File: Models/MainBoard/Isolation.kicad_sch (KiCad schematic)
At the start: 0 parts

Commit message: Save progress
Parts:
- added U2: ISO7761DW, symbol Vendor:ISO7761DW
- added U3: ISO1641DW, symbol Vendor:ISO1641DW
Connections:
- new net 3.3V_Analog: U2.16 (VCC2)
- new net 3.3V_Digital: U2.1 (VCC1), U3.3 (VCC1)
- new net 5V_Analog: U3.14 (VCC2)
- new net CS1_Analog: U2.13 (OUTC)
- new net CS1_Digital: U2.4 (INC)
- new net CS2_Analog: U2.14 (OUTB)
- new net CS2_Digital: U2.3 (INB)
- new net CS3_Analog: U2.15 (OUTA)
- new net CS3_Digital: U2.2 (INA)
- new net GND_Analog: U2.9 (GND2), U3.16 (GND2), U3.9 (GND2)
- new net GND_Digital: U2.8 (GND1), U3.1 (GND1), U3.7 (GND1)
- new net MISO_Analog: U2.10 (INF)
- new net MISO_Digital: U2.7 (OUTF)
- new net MOSI_Analog: U2.12 (OUTD)
- new net MOSI_Digital: U2.5 (IND)
- new net SCK_Analog: U2.11 (OUTE)
- new net SCK_Digital: U2.6 (INE)
- new net SCL_Analog: U3.11 (SCL2)
- new net SCL_Digital: U3.6 (SCL2)
- new net SDA_Analog: U3.12 (SDA2)
- new net SDA_Digital: U3.5 (SDA1)
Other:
- note added: "Analog / High Voltage"
- note added: "Digital"

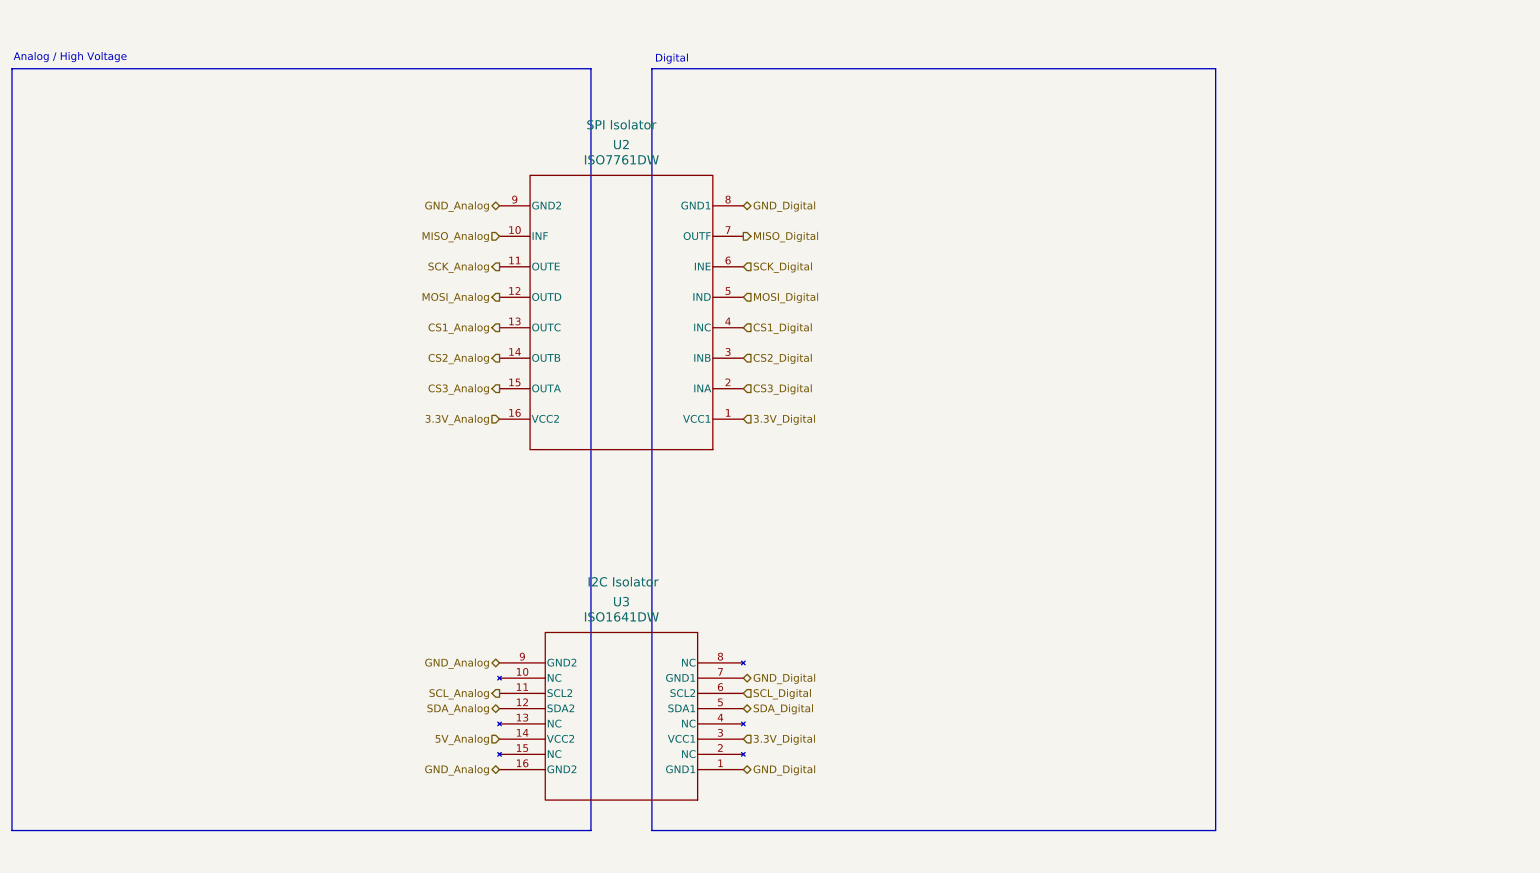
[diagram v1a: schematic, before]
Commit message: Finished the isolators
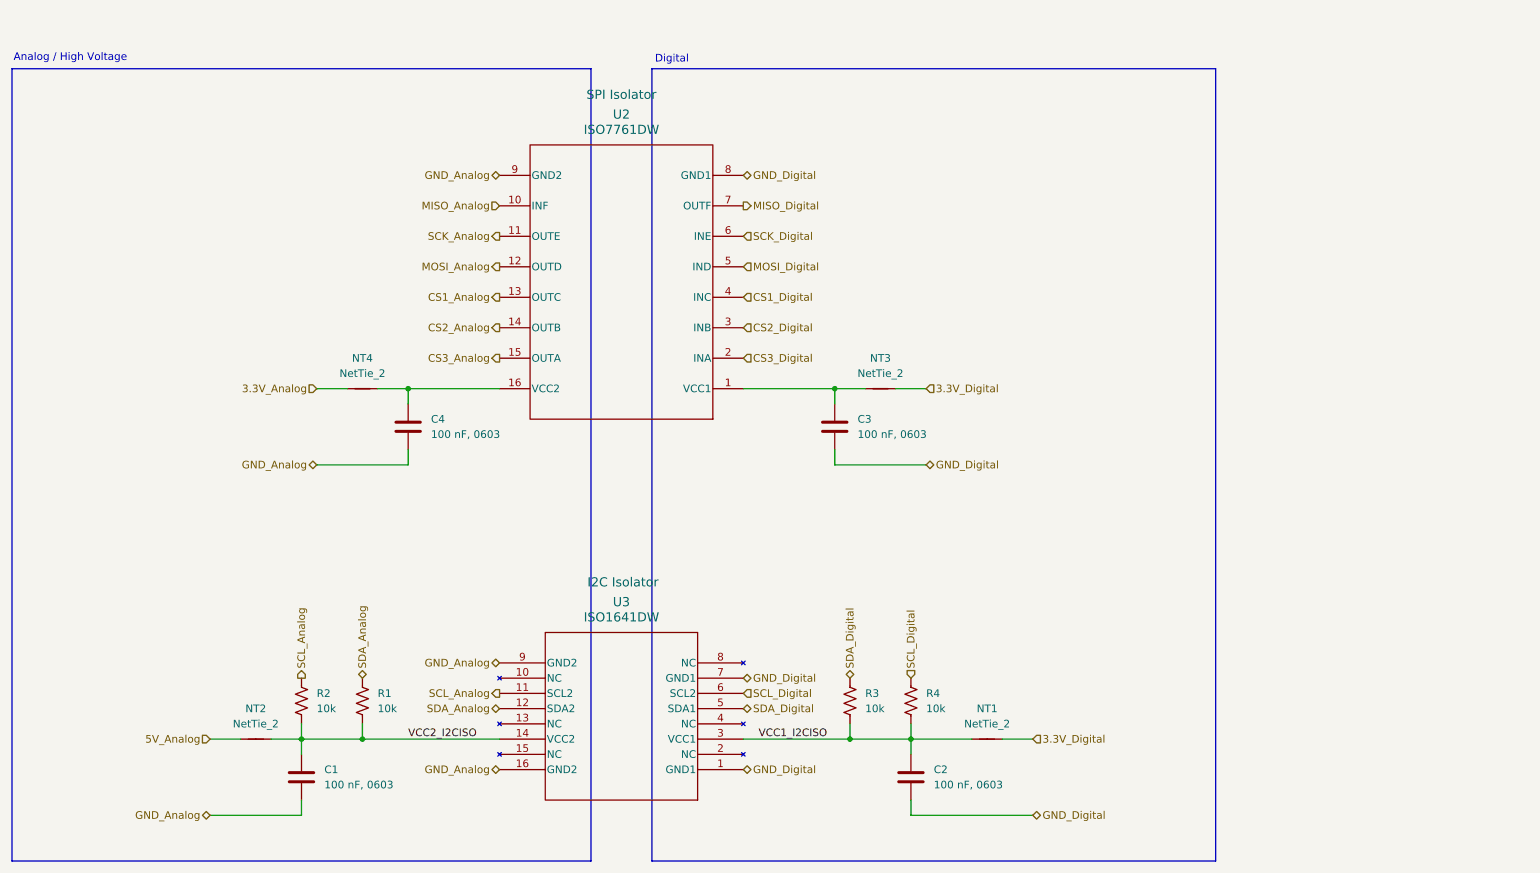
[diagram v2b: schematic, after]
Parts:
- added C1, C2, C3, C4: 100 nF, 0603, symbol Device:C
- added NT1, NT2, NT3, NT4: NetTie_2, symbol Device:NetTie_2
- added R1, R2, R3, R4: 10k, symbol Device:R_US
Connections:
- net 3.3V_Analog: now also NT4.1; no longer U2.16 (VCC2)
- net 3.3V_Digital: now also NT1.2, NT3.2; no longer U2.1 (VCC1), U3.3 (VCC1)
- net 5V_Analog: now also NT2.1; no longer U3.14 (VCC2)
- net GND_Analog: now also C1.2, C4.2
- net GND_Digital: now also C2.2, C3.2
- net SCL_Analog: now also R2.1
- net SCL_Digital: now also R4.1
- net SDA_Analog: now also R1.1
- net SDA_Digital: now also R3.1
- new net: C4.1, NT4.2, U2.16 (VCC2)
- new net: C3.1, NT3.1, U2.1 (VCC1)
- new net VCC1_I2CISO: C2.1, NT1.1, R3.2, R4.2, U3.3 (VCC1)
- new net VCC2_I2CISO: C1.1, NT2.2, R1.2, R2.2, U3.14 (VCC2)
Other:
- moved on the sheet: U2

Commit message: Save progress
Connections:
- net VCC2_SPI_ISO: now reaches C4.1, NT4.2, U2.16 (VCC2)
- net VCC1_SPI_ISO: now reaches C3.1, NT3.1, U2.1 (VCC1)
- net VCC1_I2CISO renamed VCC1_I2C_ISO
- net VCC2_I2CISO renamed VCC2_I2C_ISO
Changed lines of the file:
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@@
 		)
 	)
-	(label "VCC1_I2CISO"
+	(label "VCC2_SPI_ISO"
+		(at 91.44 78.74 0)
+		(effects
+			(font
+				(size 1.27 1.27)
+			)
+			(justify left bottom)
+		)
+	)
+	(label "VCC1_I2C_ISO"
 		(at 149.86 137.16 0)
 		(effects
@@
 		)
 	)
-	(label "VCC2_I2CISO"
+	(label "VCC2_I2C_ISO"
 		(at 91.44 137.16 0)
 		(effects
 			(font
+				(size 1.27 1.27)
+			)
+			(justify left bottom)
+		)
+	)
+	(label "VCC1_SPI_ISO"
+		(at 149.86 78.74 0)
+		(effects
+			(font

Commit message: Finished the DACs
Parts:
- R1, R2, R3, R4: value 10k -> 10k, 1%
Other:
- moved on the sheet: C1, C2, NT1, NT2, R1, R2, R4

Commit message: Save progress
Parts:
- removed NT1, NT2, NT3, NT4: NetTie_2, symbol Device:NetTie_2
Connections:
- net VCC1_I2C_ISO is gone; now on net 3.3V_Digital: C2.1, R3.2, R4.2, U3.3 (VCC1)
- net VCC1_SPI_ISO is gone; now on net 3.3V_Digital: C3.1, U2.1 (VCC1)
- net VCC2_I2C_ISO is gone; now on net 5V_Analog: C1.1, R1.2, R2.2, U3.14 (VCC2)
- net VCC2_SPI_ISO is gone; now on net 3.3V_Analog: C4.1, U2.16 (VCC2)

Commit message: Save progress
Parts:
- added NT1, NT2, NT3, NT4: NetTie_2, symbol Device:NetTie_2
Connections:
- net 3.3V_Analog: now also NT4.1; no longer C4.1, U2.16 (VCC2)
- net 3.3V_Digital: now also NT2.2, NT3.2; no longer C2.1, C3.1, R3.2, R4.2, U2.1 (VCC1), U3.3 (VCC1)
- net 5V_Analog: now also NT1.1; no longer C1.1, R1.2, R2.2, U3.14 (VCC2)
- new net VCC1_I2C: C2.1, NT2.1, R3.2, R4.2, U3.3 (VCC1)
- new net VCC1_SPI: C3.1, NT3.1, U2.1 (VCC1)
- new net VCC2_I2C: C1.1, NT1.2, R1.2, R2.2, U3.14 (VCC2)
- new net VCC2_SPI: C4.1, NT4.2, U2.16 (VCC2)

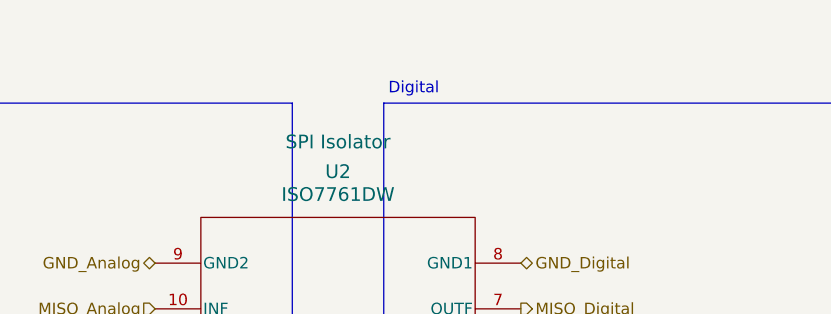
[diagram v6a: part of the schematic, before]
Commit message: Connectors should be fully specified now
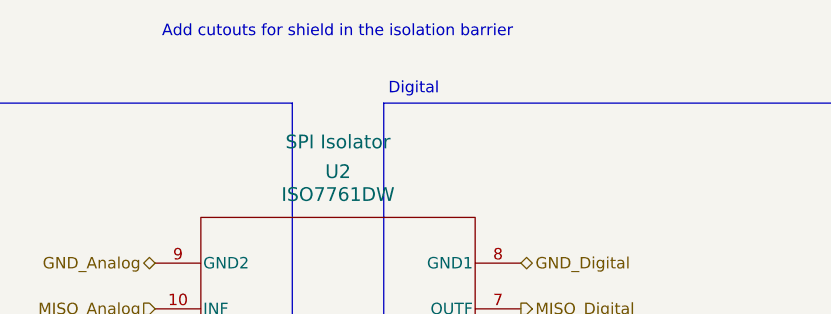
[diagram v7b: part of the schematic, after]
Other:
- note added: "Add cutouts for shield in the isolation barrier"
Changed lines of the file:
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@@
+		)
+	)
+	(text "Add cutouts for shield in the isolation barrier"
+		(exclude_from_sim no)
+		(at 107.442 16.764 0)
+		(effects
+			(font
+				(size 1.27 1.27)
+			)
+			(justify left top)
 		)
 	)

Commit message: Should be at a major turning point in the project
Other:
- note added: "Do not create cutouts for shield to be across the isolation barrier. This causes too many issues and is just a waste of time in the design phase."
- note removed: "Add cutouts for shield in the isolation barrier"
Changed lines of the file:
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@@
+		)
+	)
+	(text "Do not create cutouts for shield to be\nacross the isolation barrier. This\ncauses too many issues and is just a\nwaste of time in the design phase."
+		(exclude_from_sim no)
+		(at 232.41 26.416 0)
+		(effects
+			(font
+				(size 1.27 1.27)
+			)
+			(justify left top)
 		)
 	)
@@
 		(effects
 			(font
-				(size 1.27 1.27)
-			)
-			(justify left top)
-		)
-	)
-	(text "Add cutouts for shield in the isolation barrier"
-		(exclude_from_sim no)
-		(at 107.442 16.764 0)
-		(effects
-			(font
